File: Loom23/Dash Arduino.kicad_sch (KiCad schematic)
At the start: 0 parts

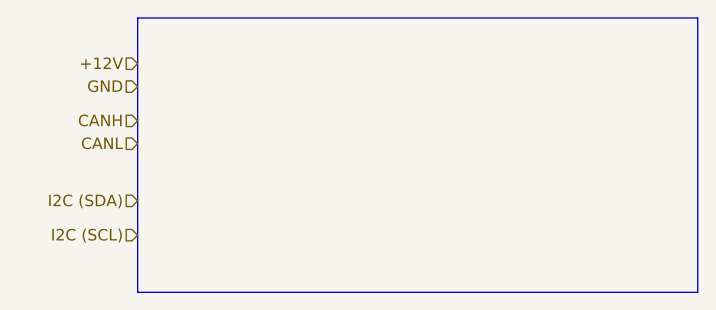
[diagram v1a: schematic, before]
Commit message: Added paddle shifter PCB and the relays.
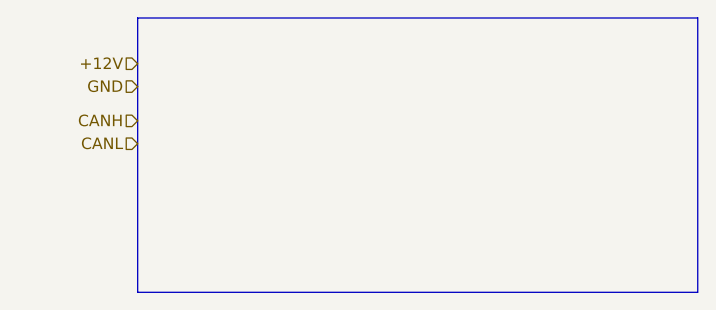
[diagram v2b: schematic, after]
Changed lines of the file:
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@@
-    (effects (font (size 1.27 1.27)) (justify right))
-  )
-  (hierarchical_label "I2C (SDA)" (shape input) (at 95.25 102.87 180)
     (effects (font (size 1.27 1.27)) (justify right))
   )
@@
     (effects (font (size 1.27 1.27)) (justify right))
   )
-  (hierarchical_label "I2C (SCL)" (shape input) (at 95.25 106.68 180)
-    (effects (font (size 1.27 1.27)) (justify right))
-  )
